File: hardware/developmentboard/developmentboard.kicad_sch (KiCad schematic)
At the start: 33 parts, among them J1 Power Header, J2 SPI Header, J3 Analog Input Header, J4 GPIO Header, U1 ADS7960, U10 DRV5053, U11 DRV5053, U12 DRV5053, U13 DRV5053, U2 DRV5053, U3 DRV5053, U4 DRV5053, U5 DRV5053, U6 DRV5053, U7 DRV5053, U8 DRV5053, U9 DRV5053

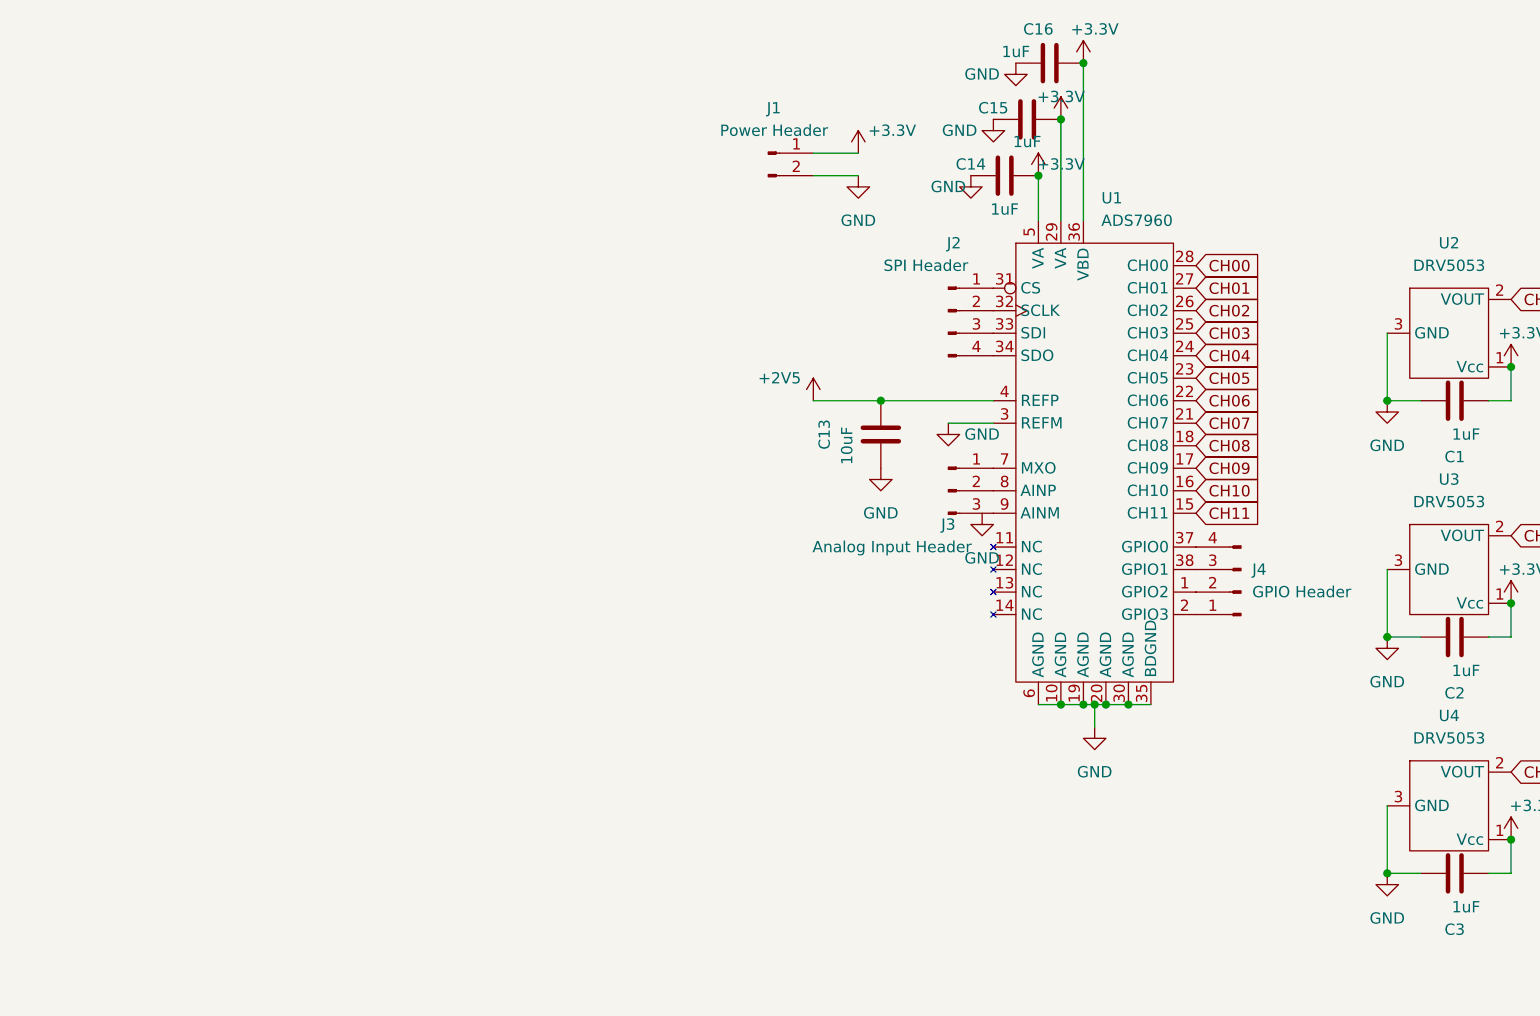
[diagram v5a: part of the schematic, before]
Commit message: Schematic Headers Added, Footprints Updated
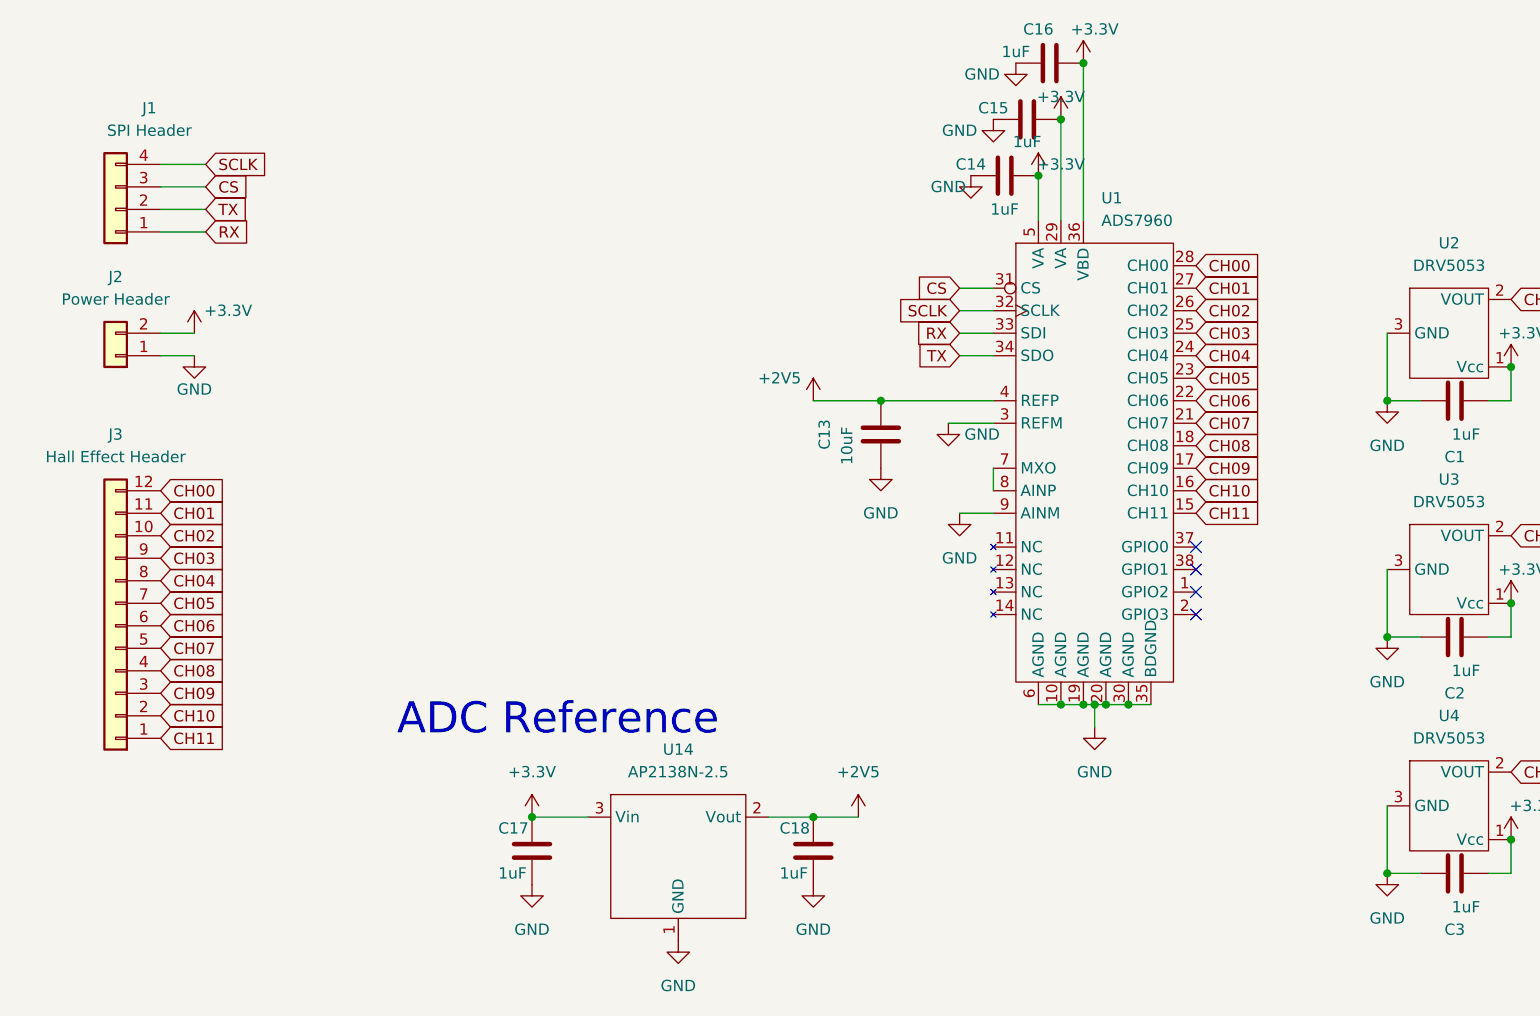
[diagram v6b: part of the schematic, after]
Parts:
- removed J1: Power Header, symbol Connector:Conn_01x02_Male
- removed J2: SPI Header, symbol Connector:Conn_01x04_Male
- removed J3: Analog Input Header, symbol Connector:Conn_01x03_Male
- removed J4: GPIO Header, symbol Connector:Conn_01x04_Male
- added C17, C18: 1uF, Capacitor_SMD:C_0603_1608Metric, symbol Device:C
- added J1: SPI Header, Connector_PinHeader_2.54mm:PinHeader_1x04_P2.54mm_Vertical, symbol Connector_Generic:Conn_01x04
- added J2: Power Header, Connector_PinHeader_2.54mm:PinHeader_1x02_P2.54mm_Vertical, symbol Connector_Generic:Conn_01x02
- added J3: Hall Effect Header, Connector_PinHeader_2.54mm:PinHeader_1x12_P2.54mm_Vertical, symbol Connector_Generic:Conn_01x12
- added U14: AP2138N-2.5, Package_TO_SOT_SMD:TSOT-23, symbol ece_capstone:AP2138N-2.5
- C1, C10, C11, C12, C13, C14, C15, C16, C2, C3, C4, C5, C6, C7, C8, C9: footprint (none) -> Capacitor_SMD:C_0603_1608Metric
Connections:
- net +2V5: now also C18.1, U14.2 (Vout)
- net +3.3V: now also C17.1, J2.2 (Pin_2), U14.3 (Vin)
- net CH00: now also J3.12 (Pin_12)
- net CH01: now also J3.11 (Pin_11)
- net CH02: now also J3.10 (Pin_10)
- net CH03: now also J3.9 (Pin_9)
- net CH04: now also J3.8 (Pin_8)
- net CH05: now also J3.7 (Pin_7)
- net CH06: now also J3.6 (Pin_6)
- net CH07: now also J3.5 (Pin_5)
- net CH08: now also J3.4 (Pin_4)
- net CH09: now also J3.3 (Pin_3)
- net CH10: now also J3.2 (Pin_2)
- net CH11: now also J3.1 (Pin_1)
- net GND: now also U1.9 (AINM), C17.2, C18.2, J2.1 (Pin_1), U14.1 (GND)
- net CS: now reaches U1.31 (CS)
- net CS: now also J1.3 (Pin_3)
- net SCLK: now reaches U1.32 (SCLK)
- net SCLK: now also J1.4 (Pin_4)
- net RX: now reaches U1.33 (SDI)
- net RX: now also J1.1 (Pin_1)
- net TX: now reaches U1.34 (SDO)
- net TX: now also J1.2 (Pin_2)
- net at U1.7 (MXO): now also U1.8 (AINP)
- no-connect marks 0 -> 4
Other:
- note added: "ADC Reference"

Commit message: cleaned up developmentboard
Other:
- note added: "ADC"
- note added: "Board I/O"
- note added: "Hall effect sensors"
- note added: "These are the 12 hall effect sensors used as keys, they must be aligned properly on PCB to be under the mechanical keys."
- company: (none) -> Landyn Francis & Jacob Mealey
- title: (none) -> MIDI Keyboard: Keyboard
- moved on the sheet: C1, C10, C11, C12, C13, C14, C15, C16, C17, C18, C2, C3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

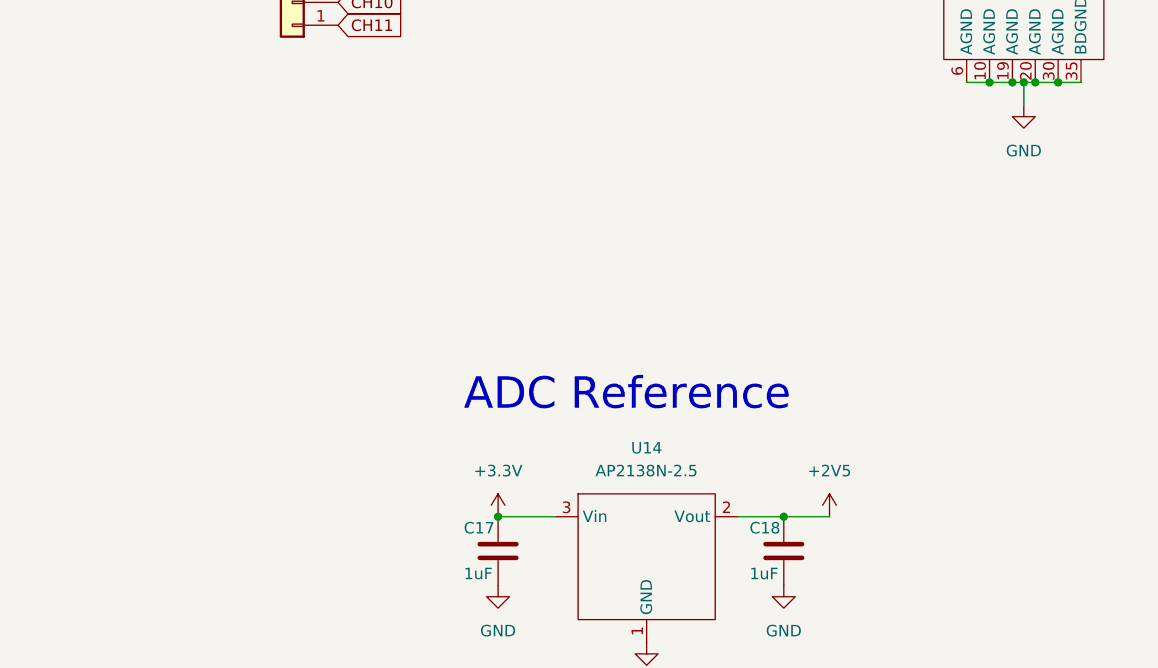
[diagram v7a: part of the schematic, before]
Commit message: Updated development board reference circuit
I threw together a circuit based on the REF5025 datasheet to replace the LDO. This is the chip that is recommended on the ADC datasheet for the reference voltage. Available on JLC as REF5025AIDR
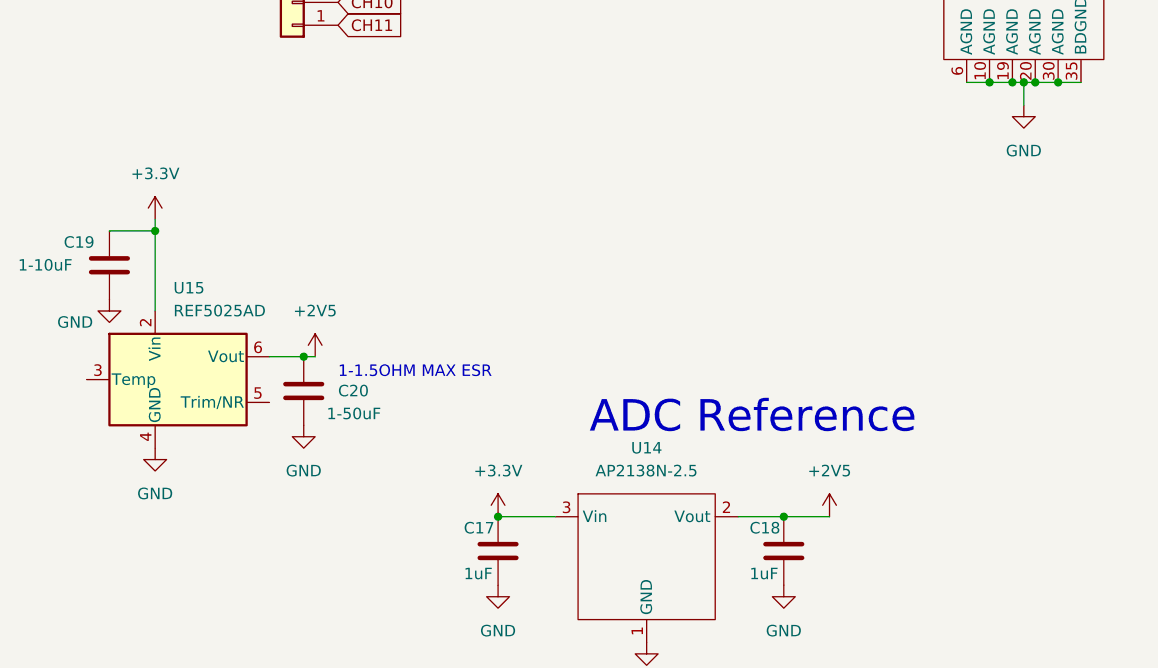
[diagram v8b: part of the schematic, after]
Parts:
- added C19: 1-10uF, symbol Device:C
- added C20: 1-50uF, symbol Device:C
- added U15: REF5025AD, Package_SO:SOIC-8_3.9x4.9mm_P1.27mm, symbol Reference_Voltage:REF5025AD
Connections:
- net +2V5: now also C20.1, U15.6 (Vout)
- net +3.3V: now also C19.1, U15.2 (Vin)
- net GND: now also C19.2, C20.2, U15.4 (GND)
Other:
- note added: "1-1.5OHM MAX ESR"
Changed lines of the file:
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@@
   (junction (at 228.6 107.95) (diameter 0) (color 0 0 0 0)
   )
+  (junction (at 52.07 144.78) (diameter 0) (color 0 0 0 0)
+  )
   (junction (at 130.81 114.3) (diameter 0) (color 0 0 0 0)
   )
@@
   )
   (junction (at 218.44 104.14) (diameter 0) (color 0 0 0 0)
+  )
+  (junction (at 35.56 130.81) (diameter 0) (color 0 0 0 0)
   )
   (junction (at 218.44 50.8) (diameter 0) (color 0 0 0 0)
@@
     (stroke (width 0) (type default) (color 0 0 0 0))
   )
+  (wire (pts (xy 48.26 144.78) (xy 52.07 144.78))
+    (stroke (width 0) (type default) (color 0 0 0 0))
+  )
   (wire (pts (xy 195.58 54.61) (xy 193.04 54.61))
     (stroke (width 0) (type default) (color 0 0 0 0))
@@
     (stroke (width 0) (type default) (color 0 0 0 0))
   )
+  (wire (pts (xy 30.48 130.81) (xy 35.56 130.81))
+    (stroke (width 0) (type default) (color 0 0 0 0))
+  )
   (wire (pts (xy 116.84 92.71) (xy 120.65 92.71))
     (stroke (width 0) (type default) (color 0 0 0 0))
@@
     (stroke (width 0) (type default) (color 0 0 0 0))
   )
+  (wire (pts (xy 52.07 144.78) (xy 53.34 144.78))
+    (stroke (width 0) (type default) (color 0 0 0 0))
+  )
   (wire (pts (xy 185.42 81.28) (xy 181.61 81.28))
     (stroke (width 0) (type default) (color 0 0 0 0))
@@
     (stroke (width 0) (type default) (color 0 0 0 0))
   )
+  (wire (pts (xy 35.56 129.54) (xy 35.56 130.81))
+    (stroke (width 0) (type default) (color 0 0 0 0))
+  )
   (wire (pts (xy 55.88 62.23) (xy 58.42 62.23))
+    (stroke (width 0) (type default) (color 0 0 0 0))
+  )
+  (wire (pts (xy 35.56 130.81) (xy 35.56 139.7))
     (stroke (width 0) (type default) (color 0 0 0 0))
   )
@@
     (effects (font (size 3 3)) (justify left bottom))
   )
-  (text "ADC Reference" (at 69.85 151.13 0)
+  (text "ADC Reference" (at 83.82 153.67 0)
     (effects (font (size 3.5 3.5)) (justify left bottom))
+  )
+  (text "1-1.5OHM MAX ESR" (at 55.88 147.32 0)
+    (effects (font (size 1.27 1.27)) (justify left bottom))
   )
   (text "These are the 12 hall effect sensors used as keys,\nthey must be aligned properly on PCB to be under\nthe mechanical keys. "
@@
     (pin "1")
   )
+  (symbol (lib_id "power:GND") (at 35.56 154.94 0) (unit 1)
+    (in_bom yes) (on_board yes) (fields_autoplaced)
+    (property "Reference" "#PWR039" (id 0) (at 35.56 161.29 0)
+      (effects (font (size 1.27 1.27)) hide)
+    )
+    (property "Value" "GND" (id 1) (at 35.56 160.02 0))
+    (property "Footprint" "" (id 2) (at 35.56 154.94 0)
+      (effects (font (size 1.27 1.27)) hide)
+    )
+    (property "Datasheet" "" (id 3) (at 35.56 154.94 0)
+      (effects (font (size 1.27 1.27)) hide)
+    )
+    (pin "1")
+  )
+  (symbol (lib_id "power:+3.3V") (at 35.56 129.54 0) (unit 1)
+    (in_bom yes) (on_board yes) (fields_autoplaced)
+    (property "Reference" "#PWR038" (id 0) (at 35.56 133.35 0)
+      (effects (font (size 1.27 1.27)) hide)
+    )
+    (property "Value" "+3.3V" (id 1) (at 35.56 124.46 0))
+    (property "Footprint" "" (id 2) (at 35.56 129.54 0)
+      (effects (font (size 1.27 1.27)) hide)
+    )
+    (property "Datasheet" "" (id 3) (at 35.56 129.54 0)
+      (effects (font (size 1.27 1.27)) hide)
+    )
+    (pin "1")
+  )
   (symbol (lib_id "power:GND") (at 118.11 54.61 0) (unit 1)
     (in_bom yes) (on_board yes)
@@
     )
     (property "Datasheet" "" (id 3) (at 107.95 87.63 0)
+      (effects (font (size 1.27 1.27)) hide)
+    )
+    (pin "1")
+  )
+  (symbol (lib_id "power:GND") (at 30.48 138.43 0) (unit 1)
+    (in_bom yes) (on_board yes)
+    (property "Reference" "#PWR037" (id 0) (at 30.48 144.78 0)
+      (effects (font (size 1.27 1.27)) hide)
+    )
+    (property "Value" "GND" (id 1) (at 26.67 140.97 0))
+    (property "Footprint" "" (id 2) (at 30.48 138.43 0)
+      (effects (font (size 1.27 1.27)) hide)
+    )
+    (property "Datasheet" "" (id 3) (at 30.48 138.43 0)
       (effects (font (size 1.27 1.27)) hide)
     )
@@
     (pin "1")
   )
+  (symbol (lib_id "power:GND") (at 52.07 152.4 0) (unit 1)
+    (in_bom yes) (on_board yes) (fields_autoplaced)
+    (property "Reference" "#PWR040" (id 0) (at 52.07 158.75 0)
+      (effects (font (size 1.27 1.27)) hide)
+    )
+    (property "Value" "GND" (id 1) (at 52.07 157.48 0))
+    (property "Footprint" "" (id 2) (at 52.07 152.4 0)
+      (effects (font (size 1.27 1.27)) hide)
+    )
+    (property "Datasheet" "" (id 3) (at 52.07 152.4 0)
+      (effects (font (size 1.27 1.27)) hide)
+    )
+    (pin "1")
+  )
   (symbol (lib_id "power:GND") (at 120.65 48.26 0) (unit 1)
     (in_bom yes) (on_board yes)
@@
     (pin "1")
   )
+  (symbol (lib_id "Device:C") (at 52.07 148.59 0) (unit 1)
+    (in_bom yes) (on_board yes)
+    (property "Reference" "C20" (id 0) (at 55.88 148.59 0)
+      (effects (font (size 1.27 1.27)) (justify left))
+    )
+    (property "Value" "1-50uF" (id 1) (at 54.61 151.13 0)
+      (effects (font (size 1.27 1.27)) (justify left))
+    )
+    (property "Footprint" "" (id 2) (at 53.0352 152.4 0)
+      (effects (font (size 1.27 1.27)) hide)
+    )
+    (property "Datasheet" "~" (id 3) (at 52.07 148.59 0)
+      (effects (font (size 1.27 1.27)) hide)
+    )
+    (pin "1")
+    (pin "2")
+  )
   (symbol (lib_name "DRV5053_1") (lib_id "ece_capstone:DRV5053") (at 260.35 40.64 0) (unit 1)
     (in_bom yes) (on_board yes) (fields_autoplaced)
@@
     (pin "1")
   )
+  (symbol (lib_id "Reference_Voltage:REF5025AD") (at 38.1 147.32 0) (unit 1)
+    (in_bom yes) (on_board yes) (fields_autoplaced)
+    (property "Reference" "U15" (id 0) (at 37.5794 137.16 0)
+      (effects (font (size 1.27 1.27)) (justify left))
+    )
+    (property "Value" "REF5025AD" (id 1) (at 37.5794 139.7 0)
+      (effects (font (size 1.27 1.27)) (justify left))
+    )
+    (property "Footprint" "Package_SO:SOIC-8_3.9x4.9mm_P1.27mm" (id 2) (at 36.195 153.67 0)
+      (effects (font (size 1.27 1.27) italic) (justify left) hide)
+    )
+    (property "Datasheet" "http://www.ti.com/lit/ds/symlink/ref5030.pdf" (id 3) (at 36.83 147.32 0)
+      (effects (font (size 1.27 1.27) italic) hide)
+    )
+    (pin "1")
+    (pin "2")
+    (pin "3")
+    (pin "4")
+    (pin "5")
+    (pin "6")
+    (pin "7")
+    (pin "8")
+  )
   (symbol (lib_id "Device:C") (at 105.41 166.37 0) (unit 1)
     (in_bom yes) (on_board yes)
@@
     (pin "2")
     (pin "3")
+  )
+  (symbol (lib_id "power:+2V5") (at 53.34 144.78 0) (unit 1)
+    (in_bom yes) (on_board yes) (fields_autoplaced)
+    (property "Reference" "#PWR041" (id 0) (at 53.34 148.59 0)
+      (effects (font (size 1.27 1.27)) hide)
+    )
+    (property "Value" "+2V5" (id 1) (at 53.34 139.7 0))
+    (property "Footprint" "" (id 2) (at 53.34 144.78 0)
+      (effects (font (size 1.27 1.27)) hide)
+    )
+    (property "Datasheet" "" (id 3) (at 53.34 144.78 0)
+      (effects (font (size 1.27 1.27)) hide)
+    )
+    (pin "1")
   )
   (symbol (lib_id "power:GND") (at 73.66 170.18 0) (unit 1)
@@
     (pin "9")
   )
+  (symbol (lib_id "Device:C") (at 30.48 134.62 0) (unit 1)
+    (in_bom yes) (on_board yes)
+    (property "Reference" "C19" (id 0) (at 25.4 132.08 0)
+      (effects (font (size 1.27 1.27)) (justify left))
+    )
+    (property "Value" "1-10uF" (id 1) (at 20.32 134.62 0)
+      (effects (font (size 1.27 1.27)) (justify left))
+    )
+    (property "Footprint" "" (id 2) (at 31.4452 138.43 0)
+      (effects (font (size 1.27 1.27)) hide)
+    )
+    (property "Datasheet" "~" (id 3) (at 30.48 134.62 0)
+      (effects (font (size 1.27 1.27)) hide)
+    )
+    (pin "1")
+    (pin "2")
+  )
   (symbol (lib_name "DRV5053_1") (lib_id "ece_capstone:DRV5053") (at 190.5 40.64 0) (unit 1)
     (in_bom yes) (on_board yes) (fields_autoplaced)
@@
       (reference "#PWR036") (unit 1) (value "+3.3V") (footprint "")
     )
+    (path "/68e5d46e-4e49-4971-9623-c92802d08cf8"
+      (reference "#PWR037") (unit 1) (value "GND") (footprint "")
+    )
+    (path "/1b5be9a7-e986-4915-8874-f70ccad766d1"
+      (reference "#PWR038") (unit 1) (value "+3.3V") (footprint "")
+    )
+    (path "/185261d4-a9aa-4e92-ade8-5af20d1275b2"
+      (reference "#PWR039") (unit 1) (value "GND") (footprint "")
+    )
+    (path "/9144551d-9461-491f-9ccf-520e54a23d97"
+      (reference "#PWR040") (unit 1) (value "GND") (footprint "")
+    )
+    (path "/e236026a-d0a9-4bd8-9e0c-55c456afad93"
+      (reference "#PWR041") (unit 1) (value "+2V5") (footprint "")
+    )
     (path "/52be0f03-1e10-4e68-8b63-a1c50920ef8a"
       (reference "#PWR0101") (unit 1) (value "GND") (footprint "")
@@
       (reference "C18") (unit 1) (value "1uF") (footprint "Capacitor_SMD:C_0603_1608Metric")
     )
+    (path "/f6e9c87b-24f6-4288-9254-c44dca53d4ee"
+      (reference "C19") (unit 1) (value "1-10uF") (footprint "")
+    )
+    (path "/b545a864-3c9e-4894-8a24-dc831b2fea0f"
+      (reference "C20") (unit 1) (value "1-50uF") (footprint "")
+    )
     (path "/46e16f3c-0fef-40db-8460-73b8ac70c6ab"
       (reference "J1") (unit 1) (value "SPI Header") (footprint "Connector_PinHeader_2.54mm:PinHeader_1x04_P2.54mm_Vertical")
@@
       (reference "U14") (unit 1) (value "AP2138N-2.5") (footprint "Package_TO_SOT_SMD:TSOT-23")
     )
-  )
+    (path "/c152adf3-39c0-4db6-b668-6b74b95a936a"
+      (reference "U15") (unit 1) (value "REF5025AD") (footprint "Package_SO:SOIC-8_3.9x4.9mm_P1.27mm")
+    )
+  )
